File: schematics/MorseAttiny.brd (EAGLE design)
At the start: 99.1 x 99.1 mm, 12 parts, among them Q1 500mA/300V

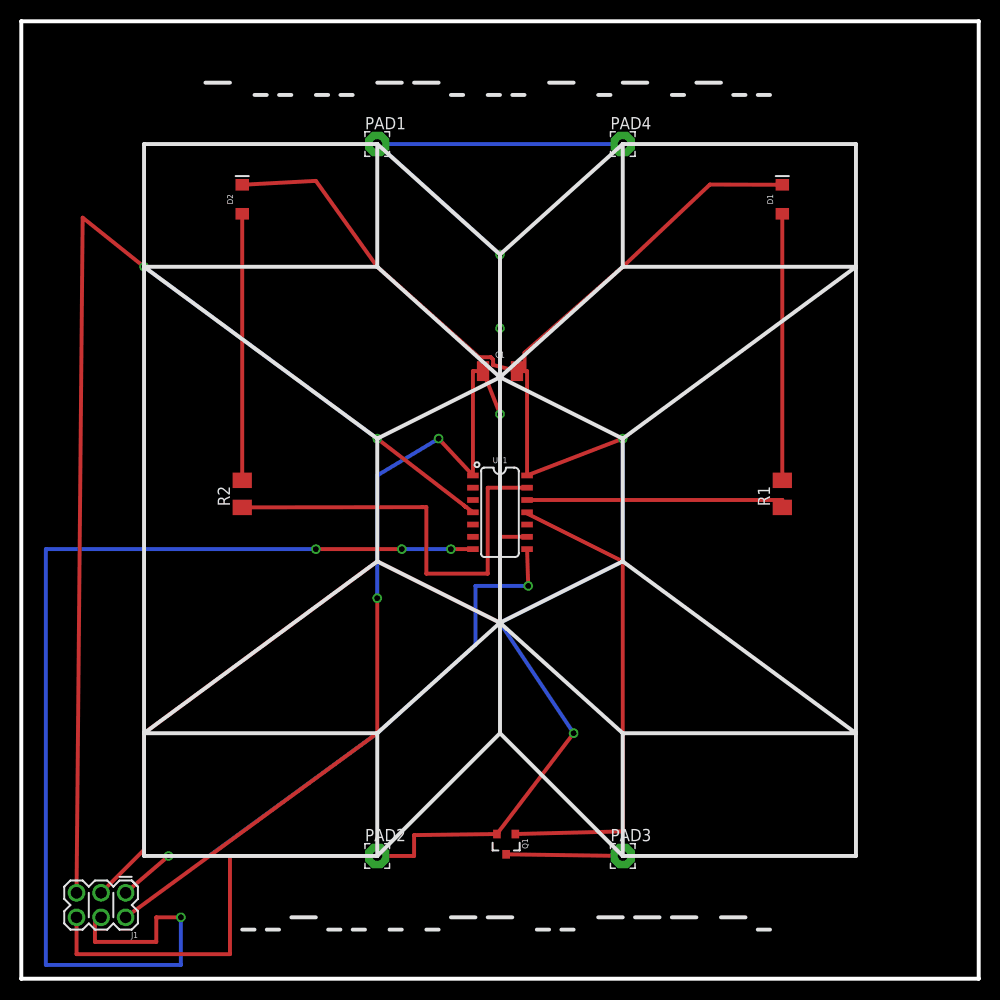
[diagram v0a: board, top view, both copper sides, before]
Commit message: New Version. Size  42.828 mm x 72.125 mm
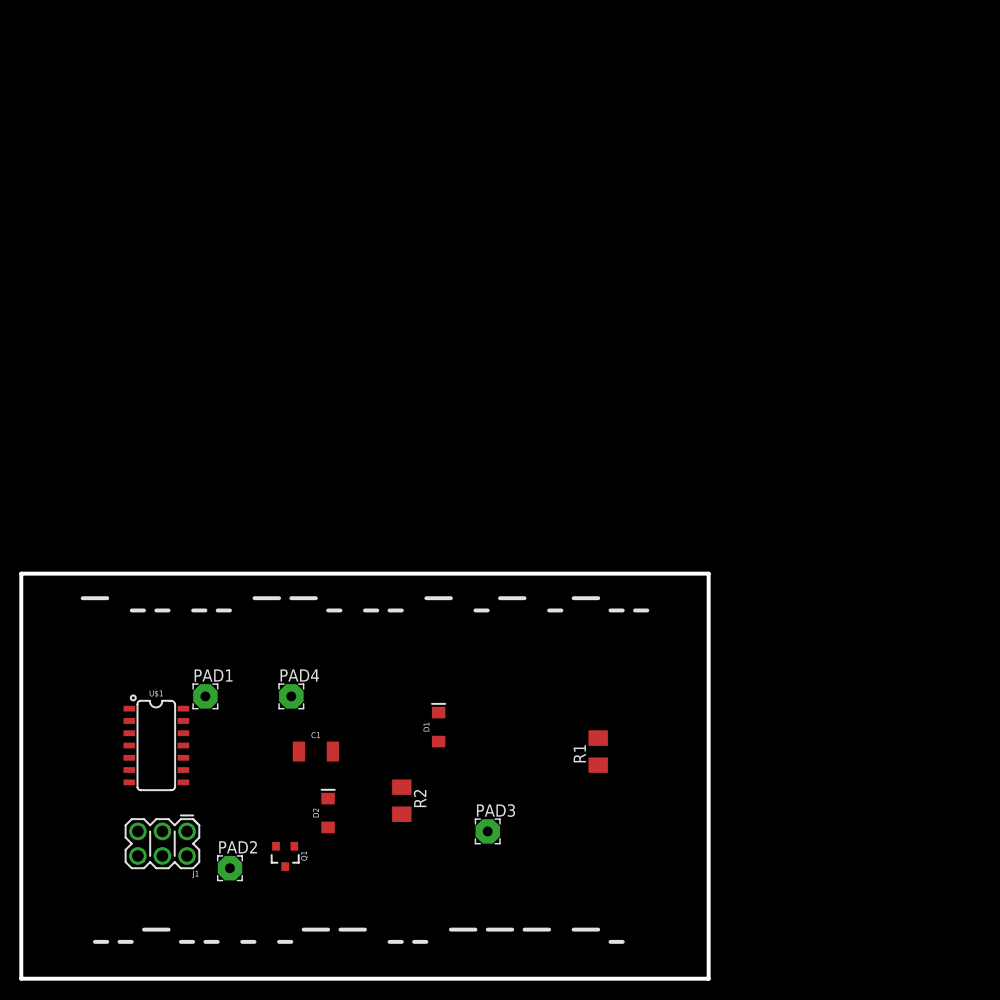
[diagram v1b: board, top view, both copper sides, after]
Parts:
- moved PAD4 66.6 mm to (27.9, 29.2)
- moved D1 65.2 mm to (43.2, 26.0)
- moved D2 64.1 mm to (31.8, 17.1)
- moved PAD1 59.9 mm to (19.1, 29.2)
- moved C1 43.7 mm to (30.5, 23.5)
- moved U$1 43.0 mm to (14.0, 24.8)
- moved R2 35.8 mm to (39.4, 18.4), turned to 270 degrees
- moved R1 32.8 mm to (59.7, 23.5)
- moved Q1 22.9 mm to (27.3, 12.7)
- moved PAD2 15.3 mm to (21.6, 11.4)
- moved PAD3 14.2 mm to (48.3, 15.2)
- moved J1 8.98 mm to (17.1, 15.2)
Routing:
- net GND: track 208.4 -> 0.00 mm, vias 2 -> 0
- net VCC: track 147.2 -> 0.00 mm, vias 5 -> 0
- net MOSI: track 120.7 -> 0.00 mm, vias 4 -> 0
- net RESET: track 120.5 -> 0.00 mm, vias 2 -> 0
- net SCK: track 74.2 -> 0.00 mm
- net MISO: track 60.6 -> 0.00 mm, vias 2 -> 0
- net N$5: track 50.7 -> 0.00 mm
- net N$1: track 45.2 -> 0.00 mm
- net N$3: track 27.6 -> 0.00 mm
- net N$2: track 27.6 -> 0.00 mm
- net N$4: track 27.2 -> 0.00 mm
- net N$7: track 12.1 -> 0.00 mm
- removed copper zone on layer 1, net GND
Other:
- board size 99.1 x 99.1 mm -> 71.1 x 41.9 mm

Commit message: NEW NEW NEEEEEEEEEEW :)
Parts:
- moved R2 33.1 mm to (7.49, 27.3)
- moved Q1 30.2 mm to (56.5, 20.3)
- moved PAD2 26.8 mm to (48.3, 8.89)
- moved D1 25.3 mm to (19.1, 18.4), turned to 180 degrees
- moved U$1 23.4 mm to (36.8, 19.7)
- moved D2 22.9 mm to (8.89, 18.4), turned to 0 degrees
- moved PAD4 17.1 mm to (44.3, 34.2)
- moved C1 15.5 mm to (17.8, 32.4), turned to 270 degrees
- moved PAD1 14.8 mm to (33.0, 34.2)
- moved PAD3 10.5 mm to (56.5, 8.76)
- moved R1 6.48 mm to (58.4, 29.8)
- moved J1 5.39 mm to (13.3, 11.4)
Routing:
- net GND: track 0.00 -> 135.2 mm
- net VCC: track 0.00 -> 96.8 mm
- net N$1: track 0.00 -> 66.1 mm, vias 0 -> 2
- net N$3: track 0.00 -> 59.4 mm, vias 0 -> 2
- net N$5: track 0.00 -> 54.0 mm
- net RESET: track 0.00 -> 47.5 mm, vias 0 -> 1
- net SCK: track 0.00 -> 45.8 mm, vias 0 -> 2
- net MISO: track 0.00 -> 33.5 mm, vias 0 -> 2
- net MOSI: track 0.00 -> 28.9 mm
- net N$4: track 0.00 -> 24.4 mm, vias 0 -> 2
- net N$7: track 0.00 -> 20.4 mm
- net N$2: track 0.00 -> 7.53 mm
- added copper zone on layer 1, net GND
